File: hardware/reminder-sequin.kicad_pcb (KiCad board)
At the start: 2 copper layers, 50 x 50 mm, 64 parts, among them J1 USB_C_Receptacle_USB2.0_16P, SW1 User, SW2 RST, SW3 BOOTSEL, U1 RP2040, U2 TPS61023DRL, U3 FM24C64B, U4 W25Q32JVSS, U5 XC6206PxxxMR, Y1 12MHz

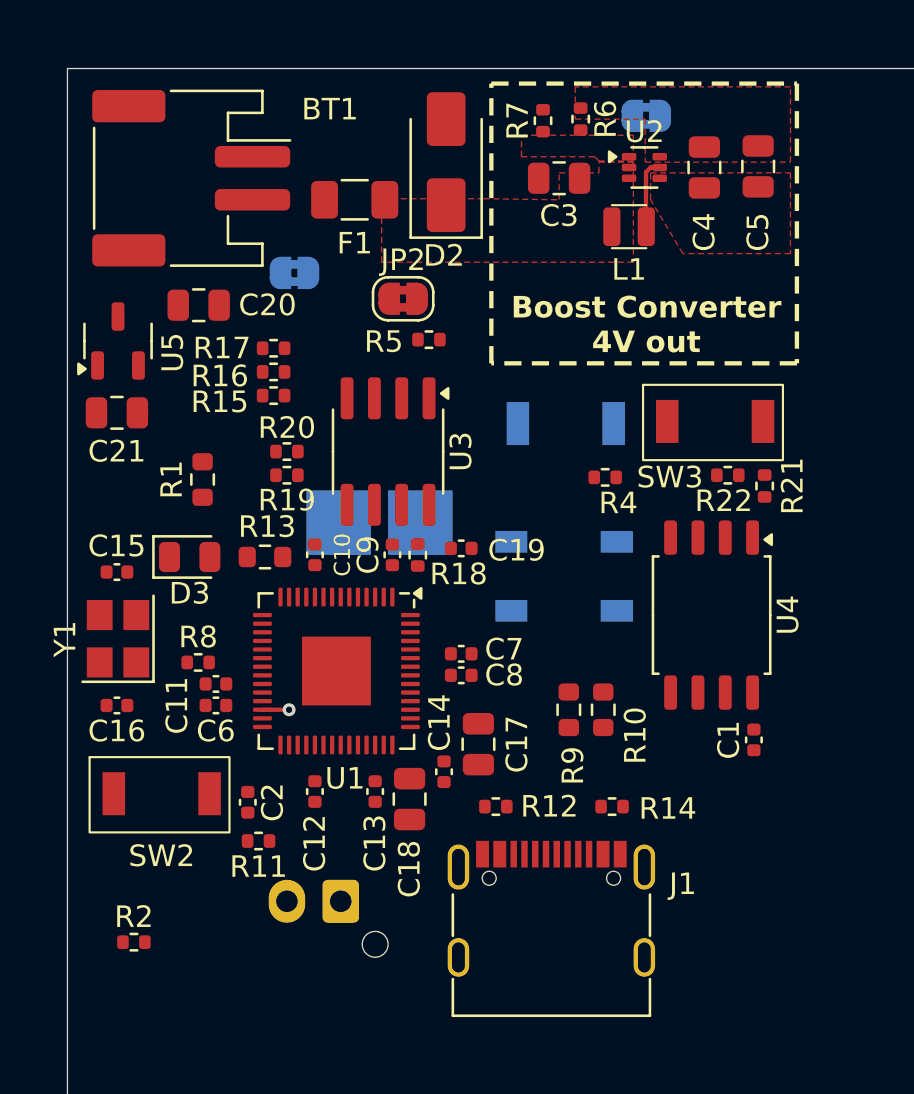
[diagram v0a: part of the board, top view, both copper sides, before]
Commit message: mounting holes
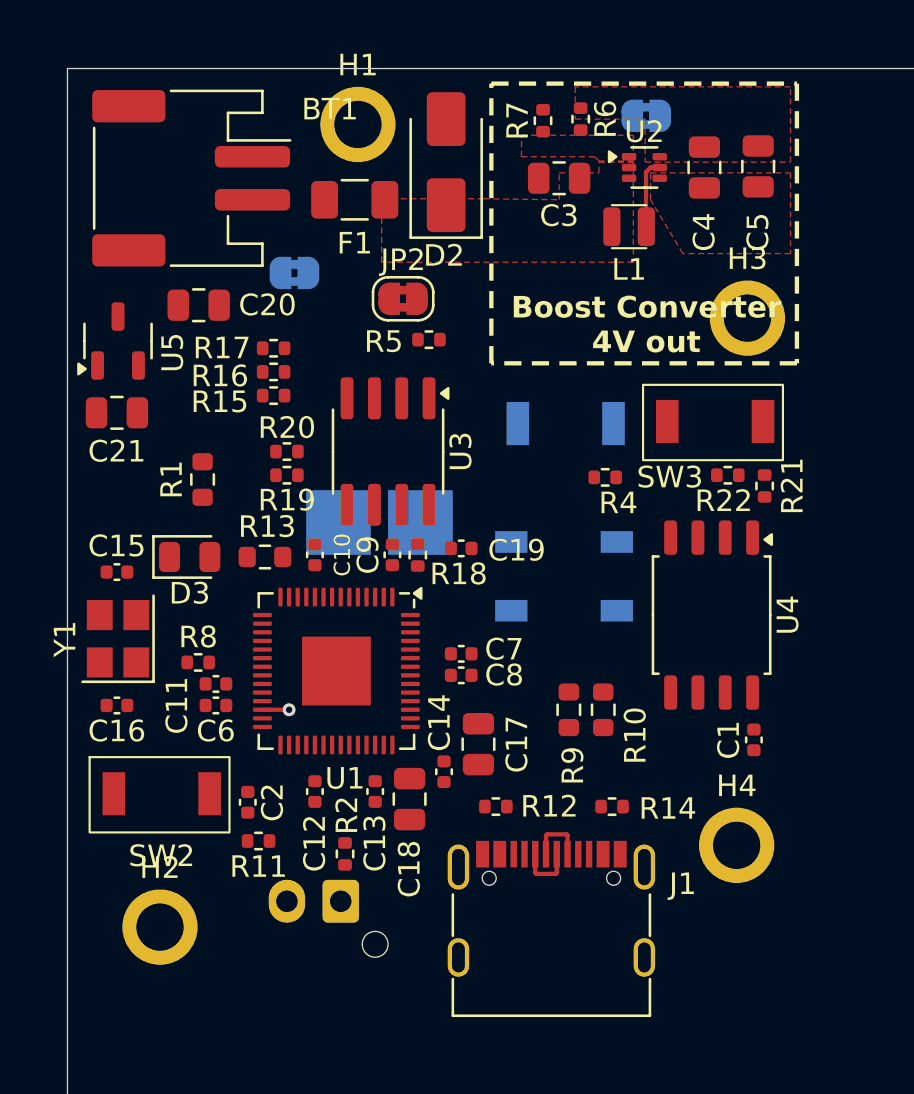
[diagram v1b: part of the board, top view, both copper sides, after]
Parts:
- added H1: MountingHole_Pad, MountingHole:MountingHole_2.2mm_M2_ISO7380_Pad, F.Cu at (164.4, 45.5)
- added H2: MountingHole_Pad, MountingHole:MountingHole_2.2mm_M2_ISO7380_Pad, F.Cu at (155.2, 82.8)
- added H3: MountingHole_Pad, MountingHole:MountingHole_2.2mm_M2_ISO7380_Pad, F.Cu at (182.5, 54.5)
- added H4: MountingHole_Pad, MountingHole:MountingHole_2.2mm_M2_ISO7380_Pad, F.Cu at (182.0, 79.0)
- moved R2 10.6 mm to (163.8, 79.4), turned to -90 degrees
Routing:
- net /USB_D-: track 0.00 -> 2.78 mm
- net /USB_D+: track 0.00 -> 2.78 mm

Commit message: started layout
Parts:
- removed C15, C16: 15pF, Capacitor_SMD:C_0402_1005Metric
- removed C17, C18, C20, C21: 1uF, Capacitor_SMD:C_0805_2012Metric
- removed C19: 0.1uF, Capacitor_SMD:C_0402_1005Metric
- removed the D2 at (168.5, 47.2)
- removed F1: Polyfuse, Fuse:Fuse_1206_3216Metric
- removed R11, R21: 1k, Resistor_SMD:R_0402_1005Metric
- removed R15, R16, R17, R19, R20: 5.1k, Resistor_SMD:R_0402_1005Metric
- removed R18, R22: 10k, Resistor_SMD:R_0402_1005Metric
- removed TP1, TP2: TestPoint, TestPoint:TestPoint_Pad_3.0x3.0mm
- added D3: GREEN, LED_SMD:LED_0805_2012Metric, F.Cu at (180.0, 71.0)
- added J2: uart, Connector_PinHeader_2.54mm:PinHeader_1x06_P2.54mm_Vertical, F.Cu at (111.9, 74.9)
- added J3: swd, Connector_PinHeader_2.54mm:PinHeader_1x06_P2.54mm_Vertical, F.Cu at (105.5, 60.4)
- BT1: value Conn_01x02 -> Battery_Cell; footprint Connector_JST:JST_PH_S2B-PH-SM4-TB_1x02-1MP_P2.00mm_Horizontal -> Battery:BatteryHolder_Keystone_3002_1x2032; moved to B.Cu
- C10, C9: value 0.1uF -> 10pF
- C11, C12: value 0.1uF -> 1uF; footprint Capacitor_SMD:C_0402_1005Metric -> Capacitor_SMD:C_0805_2012Metric
- D1: value SK6812 -> RED; footprint LED_SMD:LED_SK6812_PLCC4_5.0x5.0mm_P3.2mm -> LED_SMD:LED_0603_1608Metric; moved to F.Cu
- D2: renamed from D3; value FOR_FUNSIES -> YELLOW
- JP1, JP3, SW1: moved to F.Cu
- R1: value 500R -> 10k; footprint Resistor_SMD:R_0603_1608Metric -> Resistor_SMD:R_0402_1005Metric
- R10: value 27 -> 470; footprint Resistor_SMD:R_0603_1608Metric -> Resistor_SMD:R_0402_1005Metric
- R3: footprint Connector_JST:JST_XH_B2B-XH-AM_1x02_P2.50mm_Vertical -> LED_THT:LED_D5.0mm_FlatTop; moved to F.Cu
- R4: value 1k -> 10k
- R8: value 1k -> 150
- R9: value 27 -> 240
- SW3: value BOOTSEL -> Vibration_Detect; footprint cat:TS-1088-AR02016 -> Capacitor_THT:CP_Radial_D5.0mm_P2.00mm
- U1: value RP2040 -> STM32L011F4Px; footprint Package_DFN_QFN:QFN-56-1EP_7x7mm_P0.4mm_EP3.2x3.2mm -> Package_SO:TSSOP-20_4.4x6.5mm_P0.65mm
- U3: value FM24C64B -> CH340N; footprint Package_SO:SOIC-8_3.9x4.9mm_P1.27mm -> Package_SO:SOP-8_3.9x4.9mm_P1.27mm
- U4: value W25Q32JVSS -> XC6206PxxxMR; footprint Package_SO:SOIC-8_5.23x5.23mm_P1.27mm -> Package_TO_SOT_SMD:SOT-23-3
- U5: value XC6206PxxxMR -> TOS2115ADRBT; footprint Package_TO_SOT_SMD:SOT-23-3 -> Package_SON:VSON-8-1EP_3x3mm_P0.65mm_EP1.65x2.4mm
- Y1: value 12MHz -> 32.768kHz; footprint Crystal:Crystal_SMD_Abracon_ABM8G-4Pin_3.2x2.5mm -> Crystal:Crystal_SMD_3215-2Pin_3.2x1.5mm
- moved H4 39.5 mm to (144.5, 91.2)
- moved C11 36.7 mm to (190.0, 54.0), turned to 90 degrees
- moved C12 33.9 mm to (187.8, 54.0)
- moved U3 33.5 mm to (196.2, 74.9), turned to 90 degrees
- moved C13 31.8 mm to (183.5, 50.5), turned to -90 degrees
- moved U5 31.5 mm to (184.7, 54.5)
- moved C14 29.7 mm to (185.8, 51.5), turned to 180 degrees
- moved H3 28.9 mm to (165.8, 31.0)
- moved R1 25.6 mm to (176.3, 79.0), turned to 180 degrees
- moved D2 25.1 mm to (180.0, 74.5), turned to 180 degrees
- moved BT1 24.2 mm to (180.0, 54.2), turned to 180 degrees
- moved C8 22.9 mm to (191.5, 65.7), turned to -90 degrees
- moved R2 22.8 mm to (185.9, 73.7), turned to 0 degrees
- moved SW1 22.5 mm to (178.3, 81.5), turned to 180 degrees
- moved SW3 21.0 mm to (161.5, 67.0), turned to 180 degrees
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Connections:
- net /Power/4V_REG renamed /Power/3V3_REG
- net Net-(U1-GPIO8) renamed /YELLOW
- BT1 pad 1: GND -> Net-(BT1-+)
- BT1 pad 2: Net-(BT1-Pin_2) -> GND
- C1 pad 1: GND -> +3V3
- C1 pad 2: VDD -> GND
- C10 pad 1: GND -> Net-(U1-PC15)
- C10 pad 2: VDD -> GND
- C11 pad 2: VDD -> VBUS
- C12 pad 2: VDD -> /Power/3V3_USB
- C13 pad 2: VDD -> /Power/3V3_USB
- C14 pad 2: VDD -> /Power/3V3_BATT
- C6 pad 1: GND -> +3V3
- C6 pad 2: +1V1 -> GND
- C7 pad 1: GND -> +3V3
- C7 pad 2: +1V1 -> GND
- C8 pad 1: GND -> +3V3
- C8 pad 2: VDD -> GND
- C9 pad 1: GND -> Net-(U1-PC14)
- C9 pad 2: VDD -> GND
- D1 pad 2: /LED -> Net-(D1-A)
- JP1 pad 1: Net-(BT1-Pin_2) -> Net-(BT1-+)
- JP1 pad 2: Net-(JP1-B) -> +BATT
- JP3 pad 2: +4V -> /Power/3V3_BATT
- R1 pad 1: /LED -> VDD
- R1 pad 2: /LED -> /BUTTON
- R10 pad 1: Net-(U1-USB_DP) -> Net-(U5-ILIM)
- R10 pad 2: /USB_D+ -> GND
- R4 pad 1: VDD -> +3V3
- R4 pad 2: /BUTTON -> /VIBRATION
- R5 pad 1: /Power/Battery_Sense -> /BATTERY_SENSE
- R8 pad 1: Net-(C16-Pad2) -> /RED
- R8 pad 2: Net-(U1-XOUT) -> Net-(D1-A)
- R9 pad 1: Net-(U1-USB_DM) -> /GREEN
- R9 pad 2: /USB_D- -> Net-(D3-A)
- SW3 pad 1: Net-(R21-Pad2) -> /VIBRATION
- U1 pad 1: VDD -> unconnected-(U1-PB9-Pad1)
- U1 pad 10: VDD -> /RED
- U1 pad 12: unconnected-(U1-GPIO9-Pad12) -> /GREEN
- U1 pad 15: /LED -> GND
- U1 pad 16: unconnected-(U1-GPIO13-Pad16) -> +3V3
- U1 pad 17: unconnected-(U1-GPIO14-Pad17) -> /UART_TX
- U1 pad 18: unconnected-(U1-GPIO15-Pad18) -> /UART_RX
- U1 pad 19: GND -> /SWDIO
- U1 pad 2: Net-(U1-GPIO0) -> Net-(U1-PC14)
- U1 pad 20: Net-(U1-XIN) -> /SWCLK
- U1 pad 3: Net-(U1-GPIO1) -> Net-(U1-PC15)
- U1 pad 4: /SDA -> /RESET
- U1 pad 5: /SCL -> +3V3
- U1 pad 6: /EEPROM_WP -> /PHOTORESISTOR
- U1 pad 7: unconnected-(U1-GPIO5-Pad7) -> /BATTERY_SENSE
- U1 pad 8: unconnected-(U1-GPIO6-Pad8) -> /VIBRATION
- U3 pad 1: Net-(U3-A0) -> /USB_D+
- U3 pad 2: Net-(U3-A1) -> /USB_D-
- U3 pad 3: Net-(U3-A2) -> GND
- U3 pad 4: GND -> unconnected-(U3-~{RTS}-Pad4)
- U3 pad 5: /SCL -> +3V3
- U3 pad 6: /SDA -> /UART_TX
- U3 pad 7: /EEPROM_WP -> /UART_RX
- U3 pad 8: VDD -> +3V3
- U4 pad 1: /QSPI_CS -> GND
- U4 pad 2: Net-(U1-QSPI_SD1) -> /Power/3V3_USB
- U4 pad 3: Net-(U1-QSPI_SD2) -> VBUS
- U5 pad 1: GND -> unconnected-(U5-STAT-Pad1)
- U5 pad 2: +3V3 -> unconnected-(U5-D0-Pad2)
- U5 pad 3: +4V -> GND
- Y1 pad 1: Net-(C16-Pad2) -> Net-(U1-PC15)
- Y1 pad 2: GND -> Net-(U1-PC14)
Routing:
- net /Power/3V3_USB: track 0.00 -> 20.9 mm
- net +3V3: track 0.00 -> 20.8 mm, vias 0 -> 2
- net GND: track 0.00 -> 8.07 mm, vias 0 -> 4
- net /USB_D-: track 2.78 -> 0.00 mm
- net /USB_D+: track 2.78 -> 0.00 mm
- net VBUS: track 0.00 -> 2.50 mm
- net /Power/3V3_BATT: track 0.00 -> 1.60 mm
- net Net-(U5-ILIM): track 0.00 -> 1.24 mm
- net /RESET: track 1.24 -> 0.00 mm, vias 1 -> 0
- added copper zone on In2.Cu, net +3V3
- added copper zone on In1.Cu, net GND
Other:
- copper layers 2 -> 4
- board text added: "Boost Converter 3.3V out"
- board text removed: "Boost Converter 4V out"

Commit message: bom improvements
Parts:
- removed R4: 10k, Resistor_SMD:R_0402_1005Metric
- added R11: 5.1k, Resistor_SMD:R_0402_1005Metric, F.Cu at (165.2, 66.2)
- moved J2 87.3 mm to (199.0, 69.1), turned to 180 degrees
- moved J3 64.9 mm to (168.7, 74.7), turned to -135 degrees
- moved R1 35.6 mm to (194.2, 48.2)
- moved SW1 32.9 mm to (193.8, 52.5), turned to 90 degrees
- moved SW2 27.7 mm to (171.2, 58.2), turned to 180 degrees
- moved C2 23.6 mm to (168.5, 61.0), turned to 180 degrees
- moved C9 20.3 mm to (169.8, 63.0), turned to -90 degrees
- moved R2 19.3 mm to (167.2, 68.8), turned to -90 degrees
- moved C10 18.1 mm to (169.8, 65.0), turned to 90 degrees
- moved Y1 17.3 mm to (172.0, 64.0), turned to -90 degrees
- moved R12 16.2 mm to (188.8, 66.5)
- moved R14 16.2 mm to (194.2, 66.5)
- moved J1 15.9 mm to (191.3, 72.8)
- moved C6 15.5 mm to (184.2, 66.8), turned to -90 degrees
- moved R3 14.4 mm to (164.0, 62.8), turned to 90 degrees
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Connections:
- net VDD renamed 3V3
- SW3 pad 2: GND -> +3V3
- U1 pad 10: /RED -> /PHOTORESISTOR
- U1 pad 11: /YELLOW -> /RED
- U1 pad 12: /GREEN -> /BUTTON
- U1 pad 6: /PHOTORESISTOR -> /VIBRATION
- U1 pad 7: /BATTERY_SENSE -> /YELLOW
- U1 pad 8: /VIBRATION -> /GREEN
- U1 pad 9: /BUTTON -> /BATTERY_SENSE
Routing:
- net /RESET: track 0.00 -> 28.0 mm
- net /VIBRATION: track 0.00 -> 14.4 mm
- net GND: track 8.07 -> 18.8 mm, vias 4 -> 12
- net /PHOTORESISTOR: track 0.00 -> 8.11 mm
- net +3V3: track 20.8 -> 28.7 mm, vias 2 -> 4
- net Net-(U1-PC14): track 0.00 -> 6.39 mm
- net Net-(U1-PC15): track 0.00 -> 6.34 mm
- net Net-(D1-A): track 0.00 -> 2.20 mm
- net Net-(D3-A): track 0.00 -> 1.74 mm
- net Net-(D2-A): track 0.00 -> 1.74 mm
- net 3V3: track 0.00 -> 0.99 mm, vias 0 -> 1
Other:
- board text removed: "Boost Converter 3.3V out"

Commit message: switched microcontrollers, again
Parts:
- removed C7, C8: 0.1uF, Capacitor_SMD:C_0402_1005Metric
- removed U3: CH340N, Package_SO:SOP-8_3.9x4.9mm_P1.27mm
- added C15: 0.1uF, Capacitor_SMD:C_0402_1005Metric, F.Cu at (158.2, 42.8)
- added C16: 0.1uF, Capacitor_SMD:C_0402_1005Metric, F.Cu at (158.2, 44.8)
- added C17: 0.1uF, Capacitor_SMD:C_0402_1005Metric, F.Cu at (158.2, 46.8)
- added C18: 1uF, Capacitor_SMD:C_0805_2012Metric, F.Cu at (147.7, 54.7)
- added R15: 82k, Resistor_SMD:R_0603_1608Metric, F.Cu at (151.9, 54.5)
- added R16: 33k, Resistor_SMD:R_0402_1005Metric, F.Cu at (158.2, 50.8)
- added R4: 10k, Resistor_SMD:R_0402_1005Metric, F.Cu at (158.2, 48.8)
- U1: value STM32L011F4Px -> STM32L072CBTx; footprint Package_SO:TSSOP-20_4.4x6.5mm_P0.65mm -> Package_QFP:LQFP-48_7x7mm_P0.5mm
- moved C1 56.0 mm to (133.5, 40.5)
- moved C6 56.0 mm to (134.8, 40.5)
- moved J2 39.4 mm to (162.0, 55.6)
- moved SW3 21.0 mm to (151.0, 69.5)
- moved D1 6.75 mm to (181.2, 81.5)
- moved D2 6.75 mm to (178.0, 81.5)
- moved D3 6.75 mm to (175.5, 81.5)
- moved R13 6.75 mm to (178.0, 78.0)
- moved R8 6.75 mm to (181.2, 78.0)
- moved R9 6.75 mm to (175.5, 78.0)
- moved C9 4.17 mm to (171.0, 67.0)
- moved Y1 4.17 mm to (173.2, 68.0)
- moved C10 4.17 mm to (171.0, 69.0)
- moved U1 3.81 mm to (180.0, 69.5)
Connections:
- C1 pad 1: +3V3 -> GND
- C1 pad 2: GND -> +3V3
- C6 pad 1: +3V3 -> GND
- C6 pad 2: GND -> +3V3
- U1 pad 1: unconnected-(U1-PB9-Pad1) -> +3V3
- U1 pad 10: /PHOTORESISTOR -> /VIBRATION
- U1 pad 11: /RED -> /PHOTORESISTOR
- U1 pad 12: /BUTTON -> /UART_TX
- U1 pad 13: unconnected-(U1-PA7-Pad13) -> /UART_RX
- U1 pad 14: unconnected-(U1-PB1-Pad14) -> /BATTERY_SENSE
- U1 pad 15: GND -> unconnected-(U1-PA5-Pad15)
- U1 pad 16: +3V3 -> /BUTTON
- U1 pad 17: /UART_TX -> unconnected-(U1-PA7-Pad17)
- U1 pad 18: /UART_RX -> unconnected-(U1-PB0-Pad18)
- U1 pad 19: /SWDIO -> unconnected-(U1-PB1-Pad19)
- U1 pad 2: Net-(U1-PC14) -> unconnected-(U1-PC13-Pad2)
- U1 pad 20: /SWCLK -> unconnected-(U1-PB2-Pad20)
- U1 pad 3: Net-(U1-PC15) -> Net-(U1-PC14)
- U1 pad 4: /RESET -> Net-(U1-PC15)
- U1 pad 5: +3V3 -> unconnected-(U1-PH0-Pad5)
- U1 pad 6: /VIBRATION -> unconnected-(U1-PH1-Pad6)
- U1 pad 7: /YELLOW -> /RESET
- U1 pad 8: /GREEN -> GND
- U1 pad 9: /BATTERY_SENSE -> +3V3
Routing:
- net /VIBRATION: track 14.4 -> 0.00 mm
- net +3V3: track 28.7 -> 23.3 mm
- net /RESET: track 28.0 -> 24.5 mm
- net GND: track 18.8 -> 16.9 mm, vias 12 -> 10
- net Net-(U1-PC14): track 6.39 -> 5.36 mm
- net Net-(U1-PC15): track 6.34 -> 5.33 mm

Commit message: layout stuff
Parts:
- moved R1 85.6 mm to (279.8, 44.0)
- moved C1 69.1 mm to (202.5, 37.2)
- moved C15 69.1 mm to (227.2, 39.6)
- moved C16 69.1 mm to (227.2, 41.6)
- moved C17 69.1 mm to (227.2, 43.5)
- moved C6 69.1 mm to (203.8, 37.2)
- moved H1 69.1 mm to (244.8, 26.5)
- moved H2 69.1 mm to (204.8, 69.8)
- moved H3 69.1 mm to (234.8, 27.8)
- moved H4 69.1 mm to (213.5, 88.0)
- moved R11 69.1 mm to (234.2, 63.0)
- moved R15 69.1 mm to (220.9, 51.2)
- moved R16 69.1 mm to (227.2, 47.5)
- moved R2 69.1 mm to (236.2, 65.5)
- moved R4 69.1 mm to (227.2, 45.5)
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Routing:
- net /RESET: track 24.5 -> 0.00 mm
- net +3V3: track 23.3 -> 1.85 mm, vias 4 -> 2
- net /PHOTORESISTOR: track 8.11 -> 0.00 mm
- net GND: track 16.9 -> 11.1 mm, vias 10 -> 6
- net Net-(U1-PC15): track 5.33 -> 3.29 mm

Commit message: more layout
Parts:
- moved R1 91.4 mm to (189.0, 54.8)
- moved R2 70.0 mm to (166.2, 65.8), turned to 0 degrees
- moved R11 64.3 mm to (170.0, 65.8), turned to 180 degrees
- moved C17 40.4 mm to (190.5, 60.2)
- moved R4 35.7 mm to (201.5, 70.2)
- moved C16 33.8 mm to (201.5, 63.5), turned to 180 degrees
- moved C15 29.5 mm to (203.2, 56.8), turned to 180 degrees
- moved R16 23.8 mm to (203.8, 51.0)
- moved C1 19.7 mm to (192.5, 54.2)
- moved C6 18.4 mm to (194.2, 53.0), turned to 180 degrees
- moved R15 17.2 mm to (204.0, 48.2), turned to 180 degrees
- moved H2 7.77 mm to (212.5, 70.2)
- moved C2 4.42 mm to (192.0, 64.5)
- moved R14 0.77 mm to (193.8, 52.0)
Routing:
- net +3V3: track 1.85 -> 20.6 mm, vias 2 -> 6
- net /RESET: track 0.00 -> 9.70 mm
- net GND: track 11.1 -> 18.2 mm, vias 6 -> 15
- net /USB_D-: track 0.00 -> 2.83 mm
- net /USB_D+: track 0.00 -> 2.78 mm
- net 3V3: track 0.99 -> 0.00 mm, vias 1 -> 0
